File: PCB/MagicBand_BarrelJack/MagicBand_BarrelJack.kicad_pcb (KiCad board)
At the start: 2 copper layers, 40 x 40 mm, 22 parts, among them J2 PinSocket_1x08_P2.54mm_Vertic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, J3 PinHeader_1x03_P2.54mm_Vertic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, J6 JST_PH_B3B-PH-K_1x03_P2.00mm_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, J8 PinHeader_1x02_P2.54mm_Vertic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, J9 PinHeader_2x03_P2.54mm_Vertic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, Q1 SOT-23, U1 DIP-28_W7.62mm, U2 SOT-23, Y1 Crystal_HC49-4H_Vertical

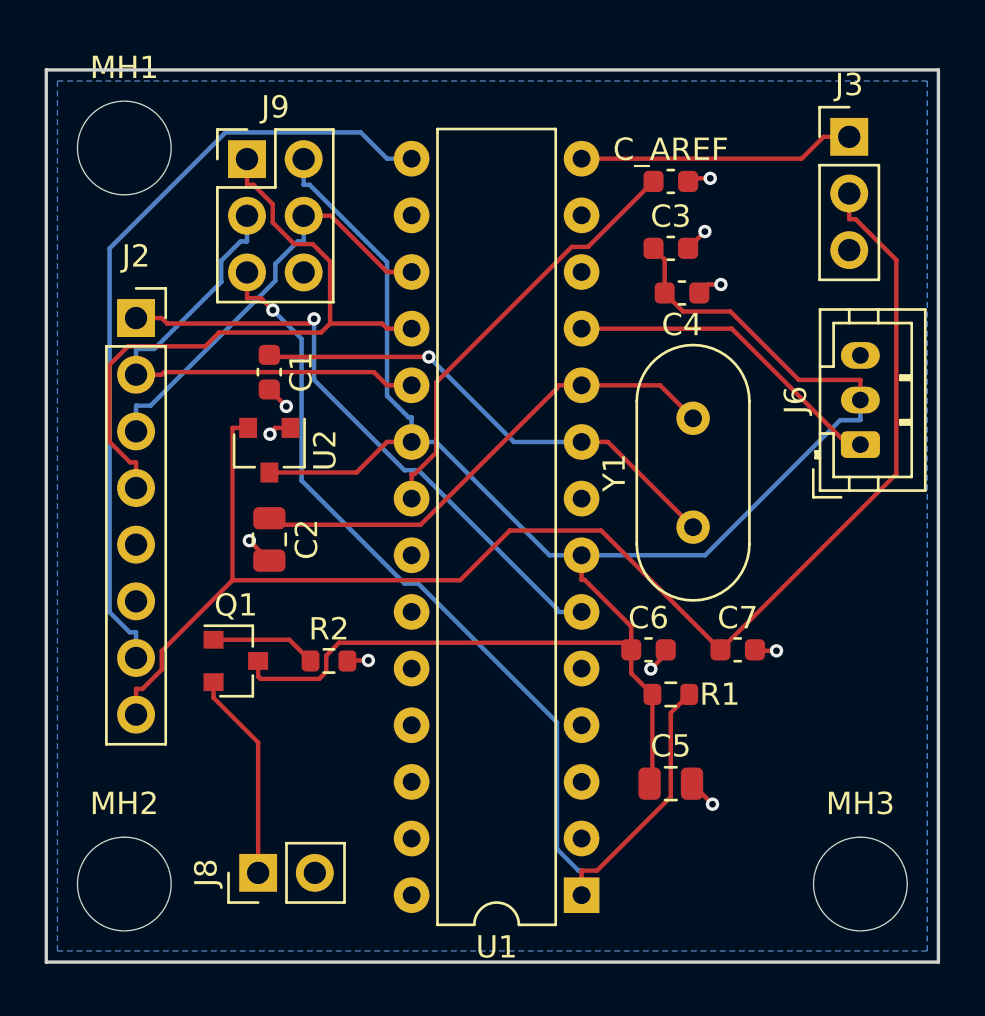
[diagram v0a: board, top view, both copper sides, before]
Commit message: J9 relocated for shrouded header, re-routed, board fully connected again
J9 moved to a spot with room for the IDC shrouded box header footprint,
old tracks/vias cleared, fresh DSN exported and FreeRouting re-run
(42 -> 0 unrouted, ~2.3s). Zones refilled.

DRC: 6 violations, same 3 real GND issues as before the move (J9 pad 6,
U1 pad 22, U1 pad 8) plus the same 4 pre-existing cosmetic warnings --
nothing new introduced by the reposition. J2 pad 6's earlier fix held.
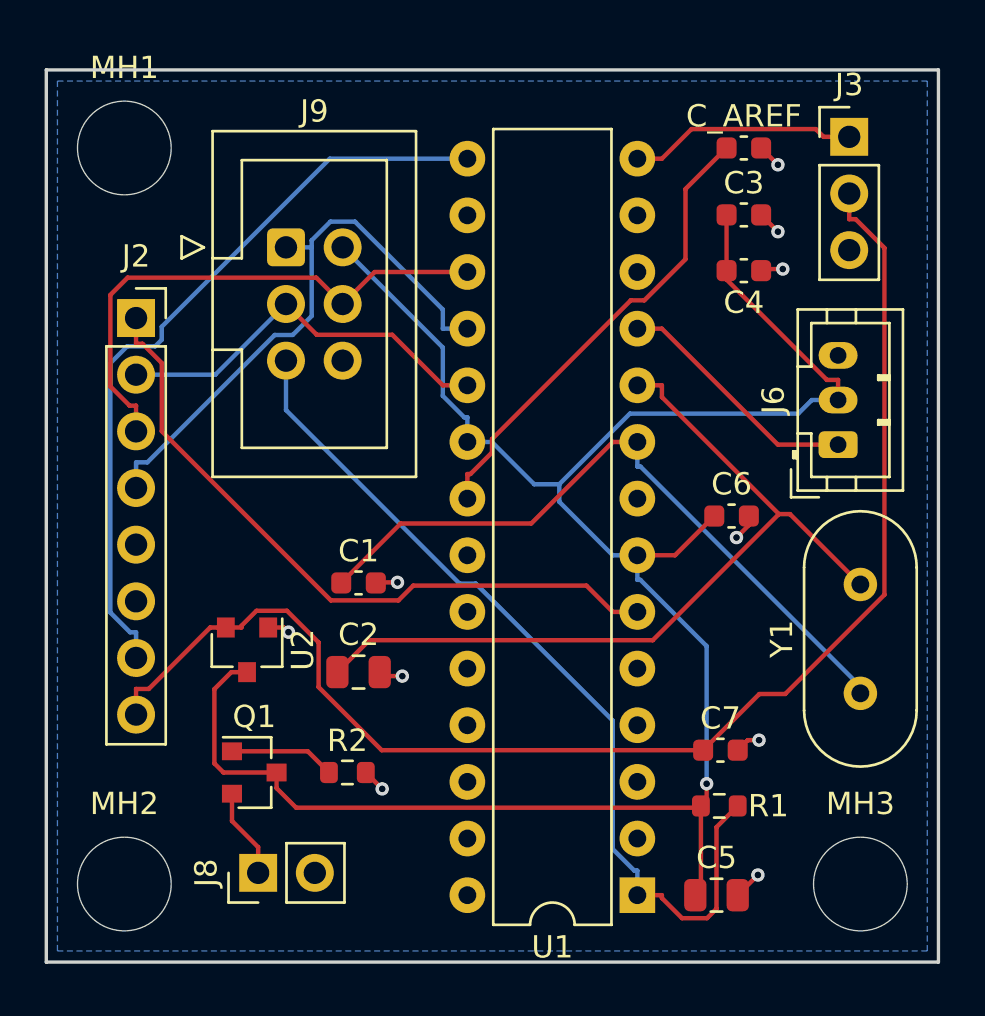
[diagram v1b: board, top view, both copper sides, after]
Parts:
- J9: value PinHeader_2x03_P2.54mm_Vertical -> IDC-Header_2x03_P2.54mm_Vertical; footprint PinHeader_2x03_P2.54mm_Vertical -> Connector_IDC:IDC-Header_2x03_P2.54mm_Vertical
- moved Y1 10.6 mm to (36.5, 27.9)
- moved C1 10.3 mm to (14.0, 23.0), turned to 0 degrees
- moved U2 9.01 mm to (9.00, 26.0)
- moved C2 7.17 mm to (14.0, 27.0), turned to 0 degrees
- moved C6 7.06 mm to (30.7, 20.0)
- moved R1 5.45 mm to (30.2, 33.0)
- moved C5 5.40 mm to (30.1, 37.0)
- moved Q1 5.07 mm to (9.32, 31.5)
- moved R2 5.07 mm to (13.5, 31.5)
- moved C7 4.57 mm to (30.2, 30.5)
- moved J9 4.32 mm to (10.7, 7.96)
- moved C3 3.60 mm to (31.3, 6.50)
- moved C_AREF 3.60 mm to (31.3, 3.50)
- moved C4 2.95 mm to (31.3, 9.00)
- moved U1 2.50 mm to (26.5, 37.0)
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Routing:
- net Net-(U1-XTAL2/PB7): track 22.4 -> 36.7 mm
- net Net-(U1-XTAL1/PB6): track 22.2 -> 31.4 mm, vias 1 -> 0
- net MCU_RESET: track 46.3 -> 40.2 mm, vias 1 -> 0
- net Net-(J8-Pin_1): track 9.38 -> 4.04 mm
- net D11: track 19.2 -> 24.2 mm
- net D13: track 22.5 -> 17.7 mm
- net D12: track 30.2 -> 26.1 mm
- net +5V: track 91.4 -> 95.2 mm, vias 0 -> 1
- net D4: track 27.3 -> 30.9 mm, vias 1 -> 0
- net +3V3: track 65.3 -> 61.7 mm
- net D5: track 14.7 -> 11.2 mm
- net D8: track 12.4 -> 10.2 mm
- net Net-(U1-AREF): track 19.2 -> 21.0 mm
- net D9: track 35.2 -> 34.0 mm

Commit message: Manual reroute resolves U1 pad 22 and J9 pad 6, board fully connected
User manually rerouted the affected nets using layer-swap (V mid-route)
after FreeRouting stalled at 6 unrouted following a placement move.
Fresh DSN exported, FreeRouting confirmed 0 unrouted nets to add.
Session imported, zones refilled.

DRC: 6 -> 5 violations, 3 -> 1 unconnected. U1 pad 22 and J9 pad 6 are
both resolved. Only U1 pad 8 (isolated island) remains from the
original 3 real GND issues, plus the same 4 pre-existing cosmetic
warnings (MH1 silk-edge clip, 3 footprint-library path warnings).
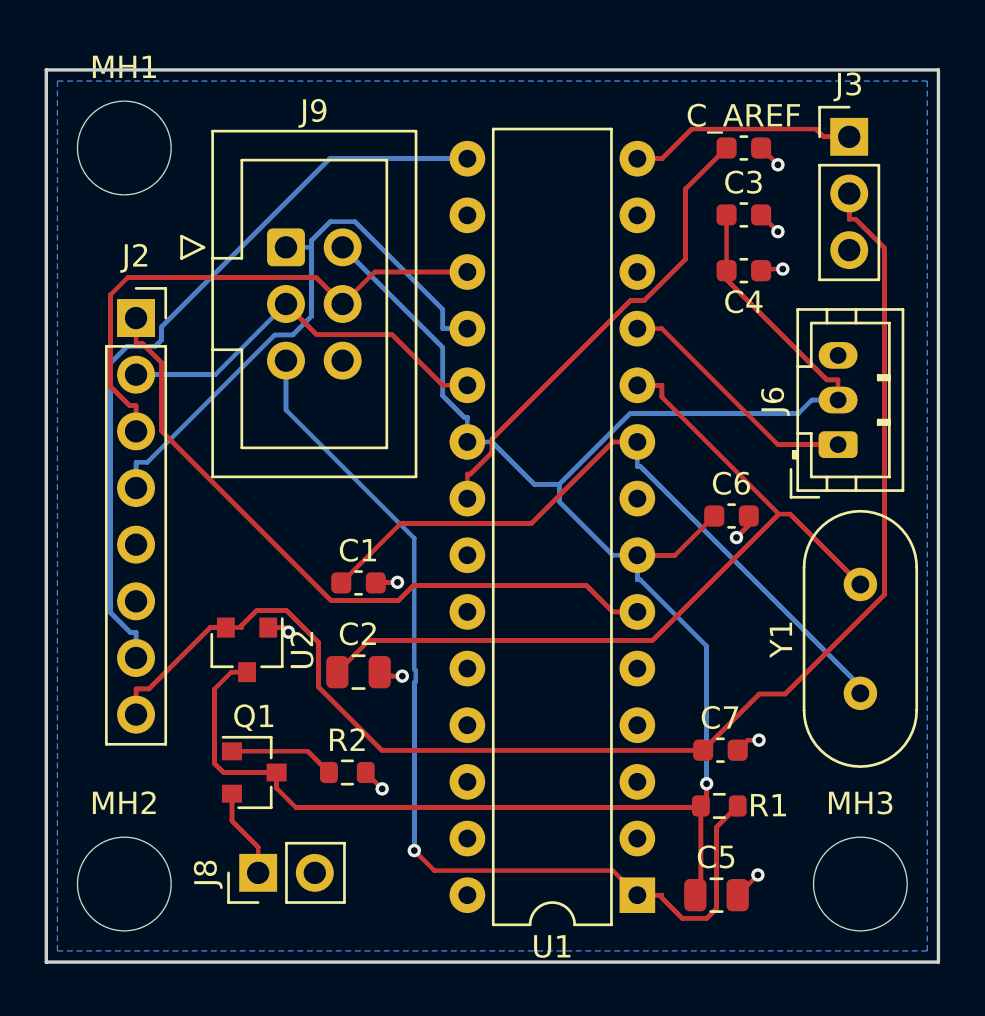
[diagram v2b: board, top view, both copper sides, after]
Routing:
- net +5V: track 95.2 -> 173.1 mm
- net +3V3: track 61.7 -> 122.0 mm
- net D9: track 34.0 -> 66.7 mm
- net D4: track 30.9 -> 60.7 mm
- net Net-(U1-XTAL2/PB7): track 36.7 -> 63.5 mm
- net Net-(U1-XTAL1/PB6): track 31.4 -> 57.8 mm
- net MCU_RESET: track 40.2 -> 63.4 mm, vias 0 -> 1
- net D11: track 24.2 -> 45.2 mm
- net Net-(U1-AREF): track 21.0 -> 40.8 mm
- net D12: track 26.1 -> 41.4 mm
- net D13: track 17.7 -> 29.8 mm
- net D8: track 10.2 -> 14.8 mm
- net GND: track 10.9 -> 14.9 mm
- net Net-(J8-Pin_1): track 4.04 -> 6.92 mm
- net D5: track 11.2 -> 13.9 mm
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
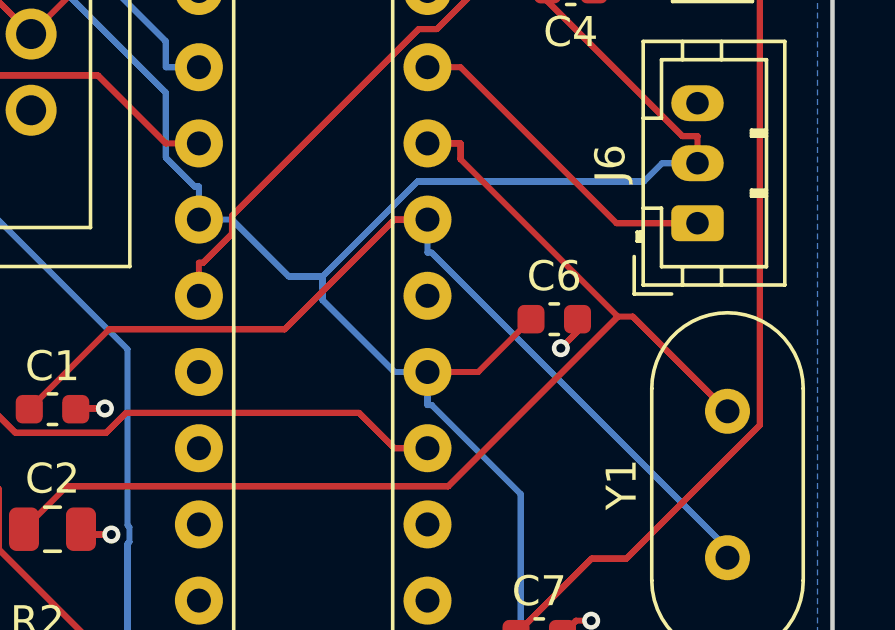
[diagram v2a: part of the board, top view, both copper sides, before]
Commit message: U1 pad 8 bridged to main GND pour, board 0 unconnected pads
Manual short track from pad 8 to the adjacent valid pour region,
bridging the isolated-island gap. DRC: 0 unconnected pads (all 3
original GND connectivity issues now resolved). 5 violations remain,
all pre-existing cosmetic (MH1 silk-edge clip, 3 footprint-library
path warnings) plus a residual starved-thermal/isolated-island flag
on pad 8 -- the pad-to-pour bond itself is still non-ideal since the
fill geometry wasn't recomputed, but the net is electrically complete
via the bridging track. Not a functional defect.
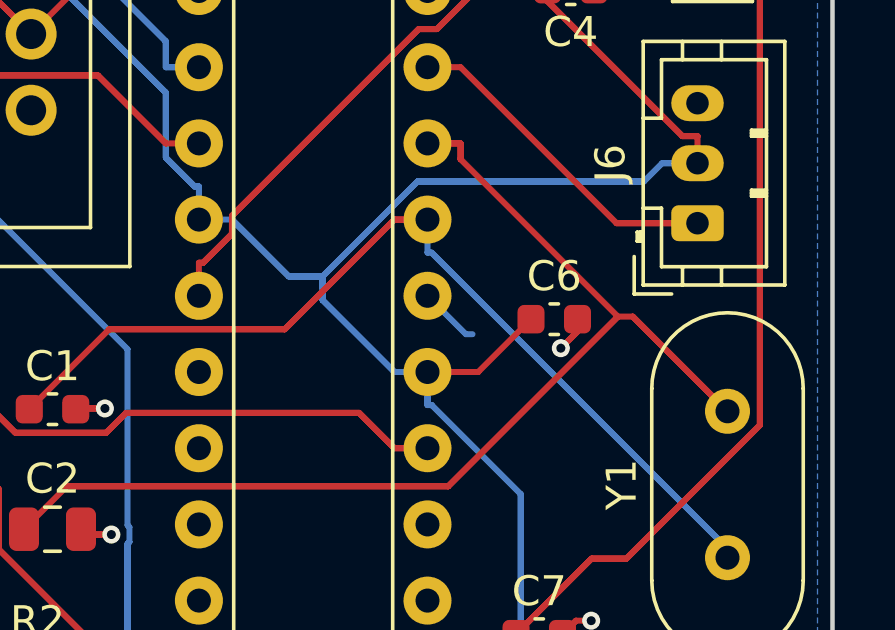
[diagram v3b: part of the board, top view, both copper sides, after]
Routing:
- net GND: track 14.9 -> 16.9 mm
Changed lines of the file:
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@@
+	)
+	(segment
+		(start 27.78 20.5)
+		(end 28 20.5)
+		(width 0.2)
+		(layer "B.Cu")
+		(net "GND")
+	)
+	(segment
+		(start 26.5 19.22)
+		(end 27.78 20.5)
+		(width 0.2)
+		(layer "B.Cu")
+		(net "GND")
 	)
 	(segment
